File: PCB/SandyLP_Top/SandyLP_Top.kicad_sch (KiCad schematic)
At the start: 37 parts

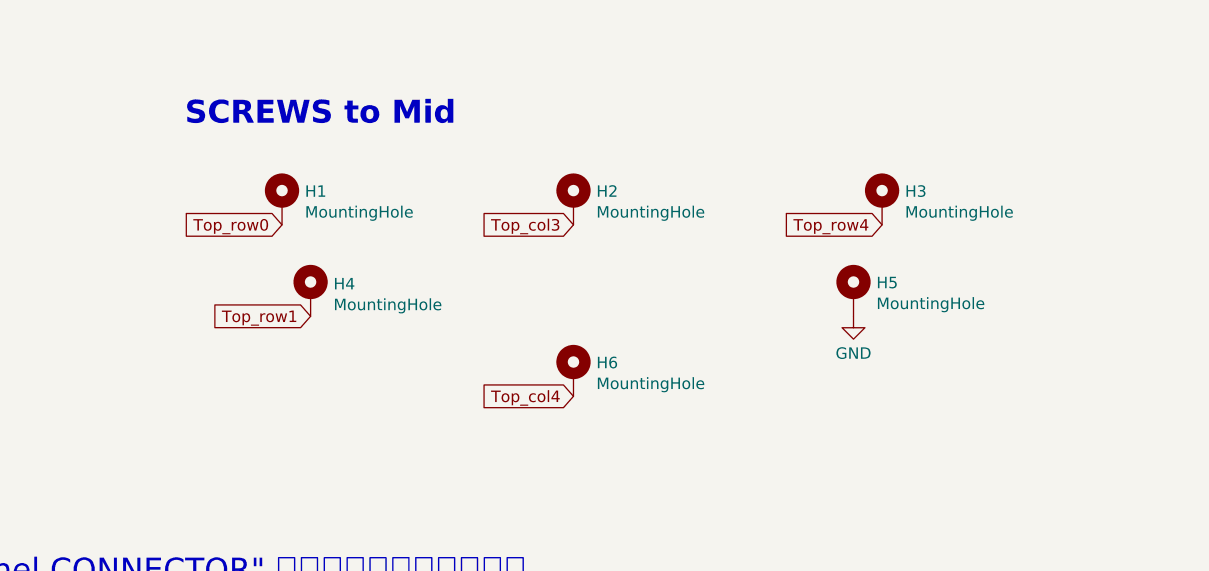
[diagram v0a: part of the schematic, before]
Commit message: スイッチの位置ずれ修正。ネジ位置調整。
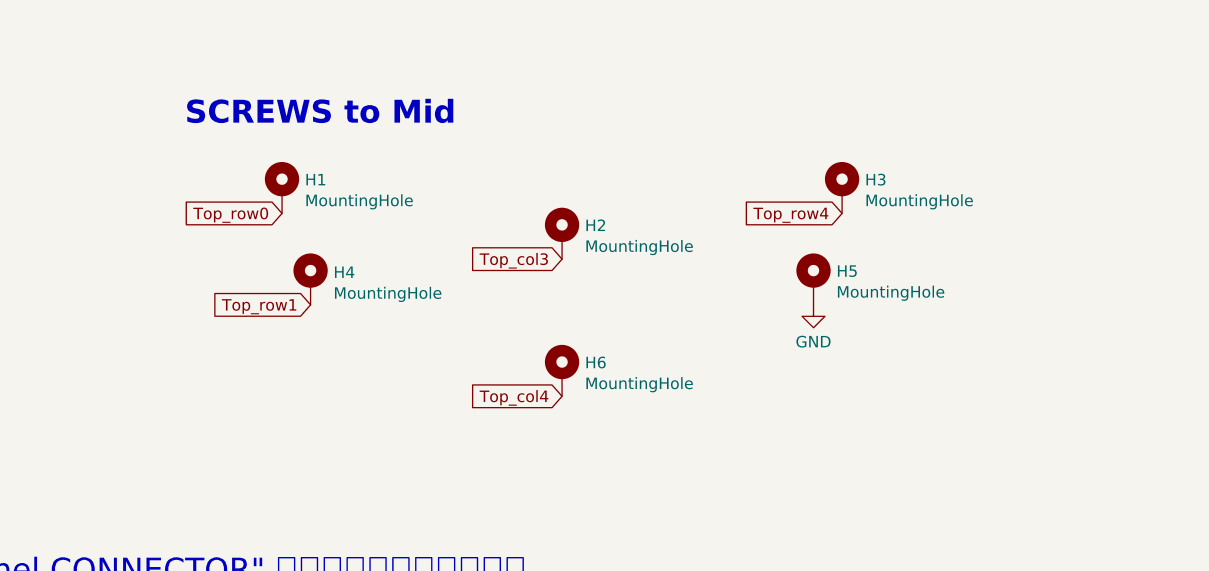
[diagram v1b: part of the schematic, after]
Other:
- moved on the sheet: H1, H2, H3, H4, H5, H6
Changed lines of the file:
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@@
 	(global_label "Top_col3"
 		(shape input)
-		(at 303.53 153.67 180)
+		(at 302.26 157.48 180)
 		(fields_autoplaced yes)
 		(effects
@@
 		)
 		(property "Intersheetrefs" "${INTERSHEET_REFS}"
-			(at 292.8535 153.67 0)
+			(at 291.5835 157.48 0)
 			(effects
 				(font
@@
 		)
 		(property "シート間のリファレンス" "${INTERSHEET_REFS}"
-			(at 303.53 155.5052 0)
+			(at 302.26 159.3152 0)
 			(effects
 				(font
@@
 	(global_label "Top_row0"
 		(shape input)
-		(at 271.145 153.67 180)
+		(at 271.145 152.4 180)
 		(fields_autoplaced yes)
 		(effects
@@
 		)
 		(property "Intersheetrefs" "${INTERSHEET_REFS}"
-			(at 234.95 31.115 0)
+			(at 234.95 29.845 0)
 			(effects
 				(font
@@
 		)
 		(property "シート間のリファレンス" "${INTERSHEET_REFS}"
-			(at 260.1122 153.5906 0)
+			(at 260.1122 152.3206 0)
 			(effects
 				(font
@@
 	(global_label "Top_row4"
 		(shape input)
-		(at 337.82 153.67 180)
+		(at 333.375 152.4 180)
 		(fields_autoplaced yes)
 		(effects
@@
 		)
 		(property "Intersheetrefs" "${INTERSHEET_REFS}"
-			(at 326.7806 153.67 0)
+			(at 322.3356 152.4 0)
 			(effects
 				(font
@@
 		)
 		(property "シート間のリファレンス" "${INTERSHEET_REFS}"
-			(at 337.82 155.5052 0)
+			(at 333.375 154.2352 0)
 			(effects
 				(font
@@
 	(global_label "Top_col4"
 		(shape input)
-		(at 303.53 172.72 180)
+		(at 302.26 172.72 180)
 		(fields_autoplaced yes)
 		(effects
@@
 		)
 		(property "Intersheetrefs" "${INTERSHEET_REFS}"
-			(at 165.735 50.165 0)
+			(at 164.465 50.165 0)
 			(effects
 				(font
@@
 		)
 		(property "シート間のリファレンス" "${INTERSHEET_REFS}"
-			(at 292.8601 172.6406 0)
+			(at 291.5901 172.6406 0)
 			(effects
 				(font
@@
 	(global_label "Top_row1"
 		(shape input)
-		(at 274.32 163.83 180)
+		(at 274.32 162.56 180)
 		(fields_autoplaced yes)
 		(effects
@@
 		)
 		(property "Intersheetrefs" "${INTERSHEET_REFS}"
-			(at 263.2806 163.83 0)
+			(at 263.2806 162.56 0)
 			(effects
 				(font
@@
 		)
 		(property "シート間のリファレンス" "${INTERSHEET_REFS}"
-			(at 274.32 165.6652 0)
+			(at 274.32 164.3952 0)
 			(effects
 				(font
@@
 	(symbol
 		(lib_id "Mechanical:MountingHole_Pad")
-		(at 337.82 151.13 0)
+		(at 333.375 149.86 0)
 		(unit 1)
 		(exclude_from_sim no)
@@
 		(dnp no)
 		(property "Reference" "H3"
-			(at 340.36 149.9616 0)
+			(at 335.915 148.6916 0)
 			(effects
 				(font
@@
 		)
 		(property "Value" "MountingHole"
-			(at 340.36 152.273 0)
+			(at 335.915 151.003 0)
 			(effects
 				(font
@@
 		)
 		(property "Footprint" "locallib:MountingHole_1.8-2.2mm_M2_Pad_minimal"
-			(at 337.82 151.13 0)
+			(at 333.375 149.86 0)
 			(effects
 				(font
@@
 		)
 		(property "Datasheet" "~"
-			(at 337.82 151.13 0)
+			(at 333.375 149.86 0)
 			(effects
 				(font
@@
 		)
 		(property "Description" ""
-			(at 337.82 151.13 0)
+			(at 333.375 149.86 0)
 			(effects
 				(font
@@
 	(symbol
 		(lib_id "Mechanical:MountingHole_Pad")
-		(at 271.145 151.13 0)
+		(at 271.145 149.86 0)
 		(unit 1)
 		(exclude_from_sim no)
@@
 		(dnp no)
 		(property "Reference" "H1"
-			(at 273.685 149.9616 0)
+			(at 273.685 148.6916 0)
 			(effects
 				(font
@@
 		)
 		(property "Value" "MountingHole"
-			(at 273.685 152.273 0)
+			(at 273.685 151.003 0)
 			(effects
 				(font
@@
 		)
 		(property "Footprint" "locallib:MountingHole_1.8-2.2mm_M2_Pad_minimal"
-			(at 271.145 151.13 0)
+			(at 271.145 149.86 0)
 			(effects
 				(font
@@
 		)
 		(property "Datasheet" "~"
-			(at 271.145 151.13 0)
+			(at 271.145 149.86 0)
 			(effects
 				(font
@@
 		)
 		(property "Description" ""
-			(at 271.145 151.13 0)
+			(at 271.145 149.86 0)
 			(effects
 				(font
@@
 	(symbol
 		(lib_id "Mechanical:MountingHole_Pad")
-		(at 303.53 151.13 0)
+		(at 302.26 154.94 0)
 		(unit 1)
 		(exclude_from_sim no)
@@
 		(dnp no)
 		(property "Reference" "H2"
-			(at 306.07 149.9616 0)
+			(at 304.8 153.7716 0)
 			(effects
 				(font
@@
 		)
 		(property "Value" "MountingHole"
-			(at 306.07 152.273 0)
+			(at 304.8 156.083 0)
 			(effects
 				(font
@@
 		)
 		(property "Footprint" "locallib:MountingHole_1.8-2.2mm_M2_Pad_minimal"
-			(at 303.53 151.13 0)
+			(at 302.26 154.94 0)
 			(effects
 				(font
@@
 		)
 		(property "Datasheet" "~"
-			(at 303.53 151.13 0)
+			(at 302.26 154.94 0)
 			(effects
 				(font
@@
 		)
 		(property "Description" ""
-			(at 303.53 151.13 0)
+			(at 302.26 154.94 0)
 			(effects
 				(font
@@
 	(symbol
 		(lib_id "Mechanical:MountingHole_Pad")
-		(at 303.53 170.18 0)
+		(at 302.26 170.18 0)
 		(unit 1)
 		(exclude_from_sim no)
@@
 		(dnp no)
 		(property "Reference" "H6"
-			(at 306.07 169.0116 0)
+			(at 304.8 169.0116 0)
 			(effects
 				(font
@@
 		)
 		(property "Value" "MountingHole"
-			(at 306.07 171.323 0)
+			(at 304.8 171.323 0)
 			(effects
 				(font
@@
 		)
 		(property "Footprint" "locallib:MountingHole_1.8-2.2mm_M2_Pad_minimal"
-			(at 303.53 170.18 0)
+			(at 302.26 170.18 0)
 			(effects
 				(font
@@
 		)
 		(property "Datasheet" "~"
-			(at 303.53 170.18 0)
+			(at 302.26 170.18 0)
 			(effects
 				(font
@@
 		)
 		(property "Description" ""
-			(at 303.53 170.18 0)
+			(at 302.26 170.18 0)
 			(effects
 				(font
@@
 	(symbol
 		(lib_id "Mechanical:MountingHole_Pad")
-		(at 274.32 161.29 0)
+		(at 274.32 160.02 0)
 		(unit 1)
 		(exclude_from_sim no)
@@
 		(dnp no)
 		(property "Reference" "H4"
-			(at 276.86 160.2486 0)
+			(at 276.86 158.9786 0)
 			(effects
 				(font
@@
 		)
 		(property "Value" "MountingHole"
-			(at 276.86 162.56 0)
+			(at 276.86 161.29 0)
 			(effects
 				(font
@@
 		)
 		(property "Footprint" "locallib:MountingHole_1.8-2.2mm_M2_Pad_minimal"
-			(at 274.32 161.29 0)
+			(at 274.32 160.02 0)
 			(effects
 				(font
@@
 		)
 		(property "Datasheet" "~"
-			(at 274.32 161.29 0)
+			(at 274.32 160.02 0)
 			(effects
 				(font
@@
 		)
 		(property "Description" ""
-			(at 274.32 161.29 0)
+			(at 274.32 160.02 0)
 			(effects
 				(font
@@
 	(symbol
 		(lib_id "power:GND")
-		(at 334.645 163.83 0)
+		(at 330.2 162.56 0)
 		(unit 1)
 		(exclude_from_sim no)
@@
 		(dnp no)
 		(property "Reference" "#PWR04"
-			(at 334.645 170.18 0)
+			(at 330.2 168.91 0)
 			(effects
 				(font
@@
 		)
 		(property "Value" "GND"
-			(at 334.645 167.9631 0)
+			(at 330.2 166.6931 0)
 			(effects
 				(font
@@
 		)
 		(property "Footprint" ""
-			(at 334.645 163.83 0)
+			(at 330.2 162.56 0)
 			(effects
 				(font
@@
 		)
 		(property "Datasheet" ""
-			(at 334.645 163.83 0)
+			(at 330.2 162.56 0)
 			(effects
 				(font
@@
 		)
 		(property "Description" "Power symbol creates a global label with name \"GND\" , ground"
-			(at 334.645 163.83 0)
+			(at 330.2 162.56 0)
 			(effects
 				(font
@@
 	(symbol
 		(lib_id "Mechanical:MountingHole_Pad")
-		(at 334.645 161.29 0)
+		(at 330.2 160.02 0)
 		(unit 1)
 		(exclude_from_sim no)
@@
 		(dnp no)
 		(property "Reference" "H5"
-			(at 337.185 160.1216 0)
+			(at 332.74 158.8516 0)
 			(effects
 				(font
@@
 		)
 		(property "Value" "MountingHole"
-			(at 337.185 162.433 0)
+			(at 332.74 161.163 0)
 			(effects
 				(font
@@
 		)
 		(property "Footprint" "locallib:MountingHole_1.8-2.2mm_M2_Pad_minimal"
-			(at 334.645 161.29 0)
+			(at 330.2 160.02 0)
 			(effects
 				(font
@@
 		)
 		(property "Datasheet" "~"
-			(at 334.645 161.29 0)
+			(at 330.2 160.02 0)
 			(effects
 				(font
@@
 		)
 		(property "Description" ""
-			(at 334.645 161.29 0)
+			(at 330.2 160.02 0)
 			(effects
 				(font
